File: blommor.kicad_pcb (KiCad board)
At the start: 2 copper layers, 66 parts, among them J1 ESP_PROG_UART, J101 Conn_01x03_Female, J102 Conn_01x03_Female, J103 Conn_01x03_Female, J104 Conn_01x03_Female, J105 Conn_01x03_Female, J2 ESP_PROG_JTAG, J3 Conn_01x02_Female, M1 Motor_DC, SW1 SW_Push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

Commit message: Added OST logo.
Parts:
- added SILKSCREEN1: OSTSymbol, SymbolOST:ost-bubble_12mm_SilkScreen, F.Cu at (114.6, 51.8)

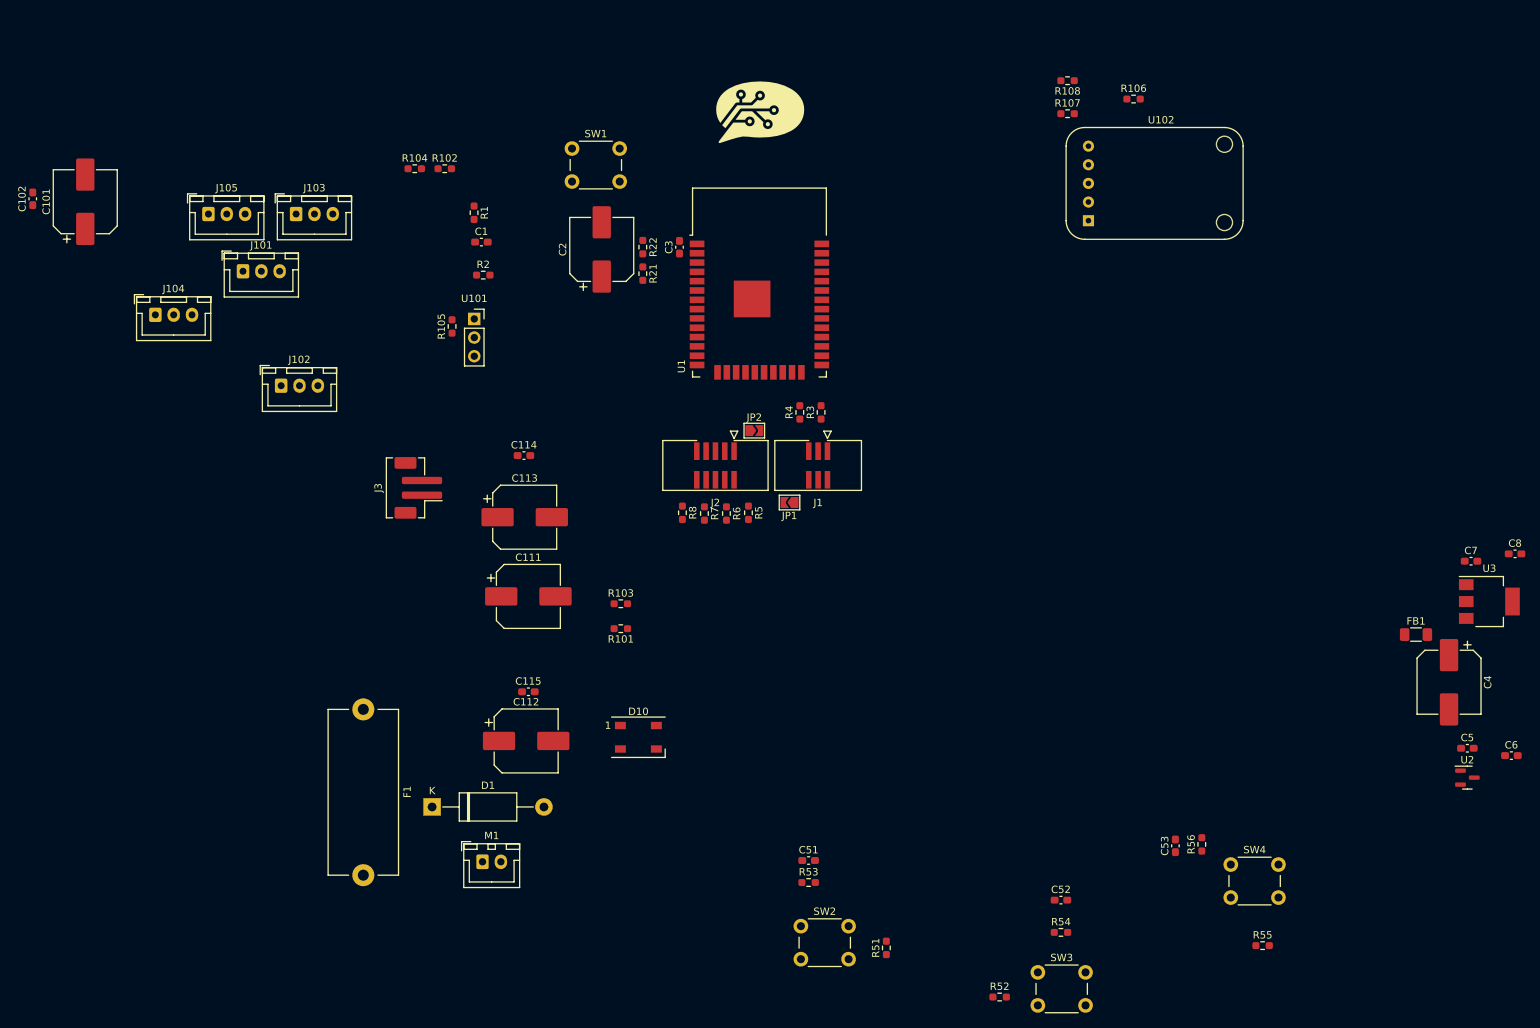
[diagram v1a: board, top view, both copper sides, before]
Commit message: Renamed ConnectorEsp folder so 3D models work. Started routing and more layout work.
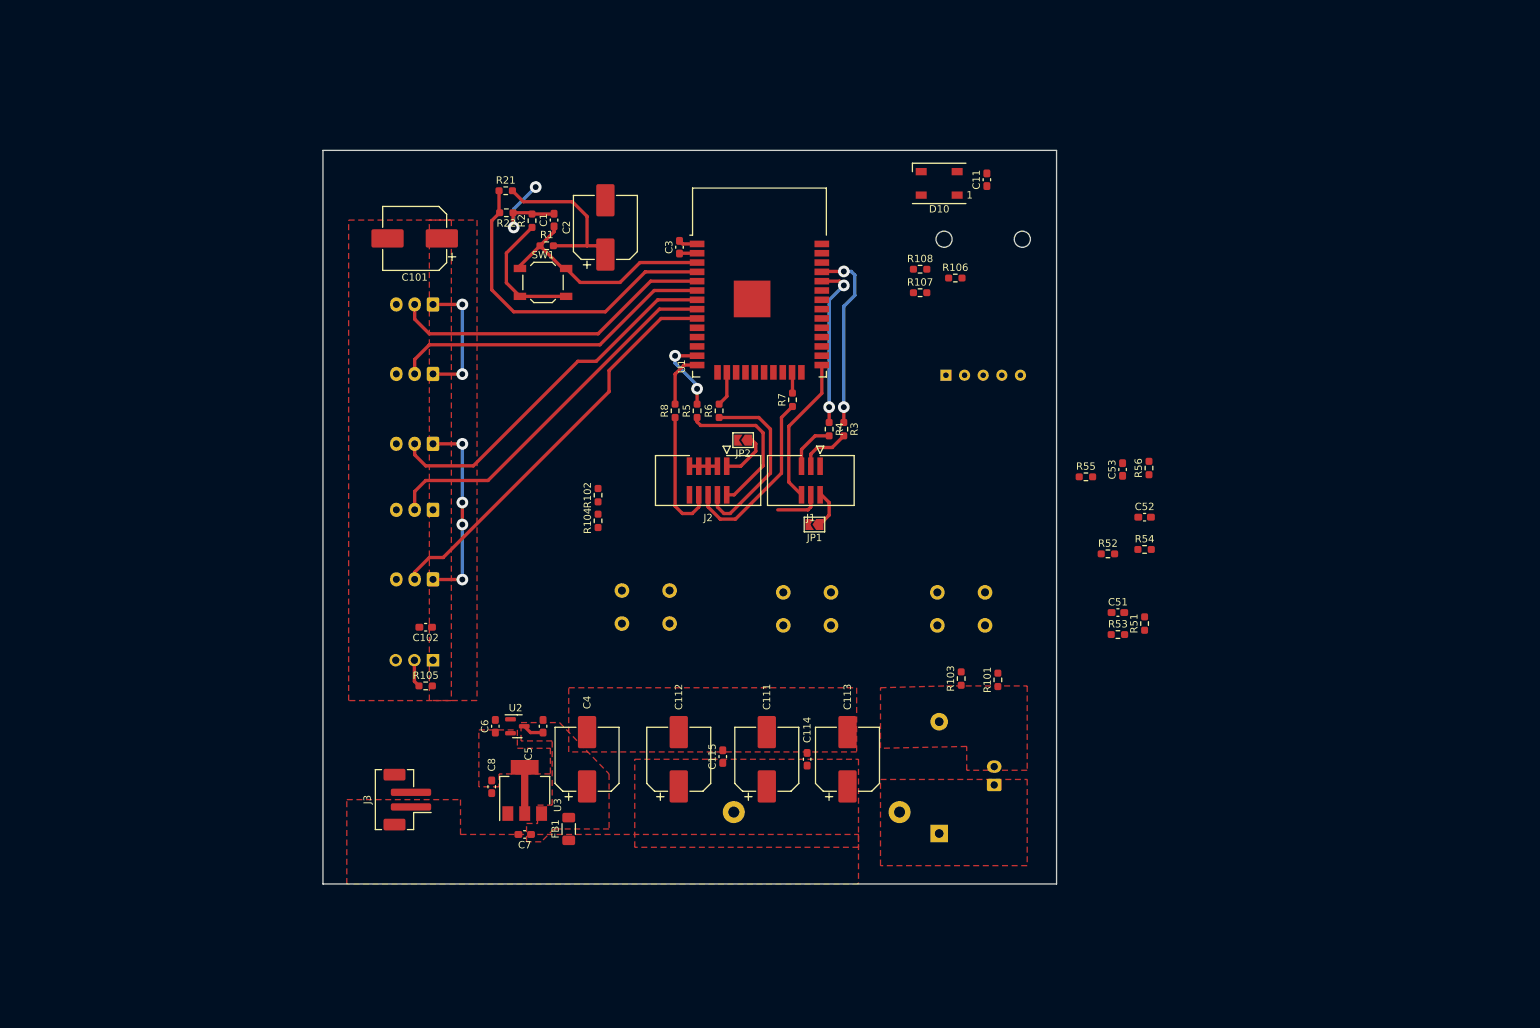
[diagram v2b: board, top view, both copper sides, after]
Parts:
- added C11: 100nF, Capacitor_SMD:C_0603_1608Metric_Pad1.08x0.95mm_HandSolder, F.Cu at (145.5, 61.0)
- D1, F1, J101, J102, J103, J104, J105, M1, SILKSCREEN1, SW2, SW3, SW4, U101, U102: moved to B.Cu
- SW1: footprint Button_Switch_THT:SW_PUSH_6mm_H5mm -> Button_Switch_SMD:SW_SPST_TL3342
- moved C8 143.1 mm to (78.0, 143.8), turned to -90 degrees
- moved C6 138.6 mm to (78.5, 135.5), turned to 90 degrees
- moved C7 134.3 mm to (82.5, 150.2), turned to 180 degrees
- moved U3 134.0 mm to (82.5, 144.2), turned to 90 degrees
- moved U2 129.7 mm to (81.5, 135.5)
- moved C5 126.0 mm to (85.0, 135.5), turned to 90 degrees
- moved FB1 118.5 mm to (88.5, 149.5), turned to 90 degrees
- moved C4 118.0 mm to (91.0, 140.0), turned to 90 degrees
- moved D10 85.9 mm to (139.0, 61.5), turned to 180 degrees
- moved C102 79.2 mm to (69.0, 122.0), turned to 180 degrees
- moved M1 70.5 mm to (146.5, 143.5), turned to 90 degrees
- moved D1 69.2 mm to (139.0, 150.1), turned to 90 degrees
- moved R55 68.3 mm to (159.0, 101.5)
- moved R52 62.2 mm to (162.0, 112.0)
- moved SW3 59.0 mm to (124.2, 117.2), turned to 180 degrees
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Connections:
- net /sensor_connector/VCC renamed /sensor_connector/SENS_VCC
- net Net-(R104-Pad1) renamed /SENSOR_POWER_EN
- U1 pad 26: unconnected-(U1-Pad26) -> MOTOR_ENABLE
- U1 pad 27: BTN_1 -> unconnected-(U1-Pad27)
- U1 pad 28: BTN_2 -> BTN_1
- U1 pad 29: unconnected-(U1-Pad29) -> BTN_2
- U1 pad 31: WS2812_DATA -> AUDIO_SD
- U1 pad 33: MOTOR_ENABLE -> ENABLE_AUDIO
- U1 pad 36: AUDIO_SD -> unconnected-(U1-Pad36)
- U1 pad 37: ENABLE_AUDIO -> WS2812_DATA
- U1 pad 6: /sensor_connector/SOIL3 -> /sensor_connector/SOIL4
- U1 pad 7: /sensor_connector/SOIL4 -> /sensor_connector/SOIL3
- U1 pad 8: /sensor_connector/SOIL1 -> /sensor_connector/SOIL2
- U1 pad 9: /sensor_connector/SOIL2 -> /sensor_connector/SOIL1
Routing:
- net /sensor_connector/SOIL1: track 0.00 -> 55.5 mm
- net /sensor_connector/SOIL2: track 0.00 -> 51.3 mm
- net /sensor_connector/SOIL3: track 0.00 -> 50.0 mm
- net Net-(U1-Pad4): track 0.00 -> 45.5 mm
- net /sensor_connector/SOIL4: track 0.00 -> 44.4 mm
- net /sensor_connector/SOIL5: track 0.00 -> 44.3 mm
- net /sensor_connector/SENS_VCC: track 0.00 -> 44.0 mm, vias 0 -> 6
- net RESET: track 0.00 -> 32.3 mm
- net +3V3: track 0.00 -> 31.9 mm
- net GND: track 0.00 -> 27.2 mm, vias 0 -> 2
- net TX: track 0.00 -> 25.4 mm, vias 0 -> 2
- net Net-(J2-Pad4): track 0.00 -> 25.2 mm
- net Net-(J2-Pad6): track 0.00 -> 24.6 mm
- net RX: track 0.00 -> 22.7 mm, vias 0 -> 2
- net Net-(J2-Pad2): track 0.00 -> 21.3 mm
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- added copper zone on F.Cu, net +3V3
- added copper zone on F.Cu, net /sensor_connector/SENS_VCC
- added copper zone on F.Cu, net GND
- added copper zone on F.Cu, net Net-(C4-Pad1)
- added copper zone on F.Cu, net Net-(D1-Pad1)
- added copper zone on F.Cu, net Net-(D1-Pad2)
- added copper zone on F.Cu, net VCC
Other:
- board outline added: 100 x 100 mm

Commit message: Typ klar nu.
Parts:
- added Q1: IPS021L, Package_TO_SOT_SMD:SOT-223-3_TabPin2, F.Cu at (129.5, 129.0)
- added Q101: A1SHB, Package_TO_SOT_SMD:SOT-23, F.Cu at (143.0, 85.0)
- added Q102: BST82-1, Package_TO_SOT_SMD:SOT-23, F.Cu at (136.5, 83.5)
- added Q2: A1SHB, Package_TO_SOT_SMD:SOT-23, F.Cu at (75.5, 118.0)
- C101, C111, C112, C113, C2, C4: footprint Capacitor_SMD:CP_Elec_8x10.5 -> Capacitor_SMD:CP_Elec_10x10.5
- moved R51 70.6 mm to (97.0, 112.5), turned to -90 degrees
- moved R53 69.9 mm to (93.5, 122.5), turned to -90 degrees
- moved C51 66.9 mm to (96.5, 122.5), turned to -90 degrees
- moved R54 52.8 mm to (115.5, 123.0), turned to -90 degrees
- moved C52 51.1 mm to (118.5, 123.0), turned to -90 degrees
- moved R52 43.0 mm to (119.0, 113.0), turned to -90 degrees
- moved R56 36.1 mm to (139.5, 123.0), turned to -90 degrees
- moved C53 35.5 mm to (136.5, 123.0), turned to -90 degrees
- moved R101 24.1 mm to (123.0, 126.5), turned to 0 degrees
- moved R55 22.4 mm to (139.5, 112.5), turned to -90 degrees
- moved R102 19.4 mm to (79.0, 118.0), turned to -90 degrees
- moved R103 18.5 mm to (123.5, 130.0)
- moved R104 14.8 mm to (79.0, 113.5), turned to -90 degrees
- moved R106 10.7 mm to (139.5, 85.0), turned to 90 degrees
- moved SW2 9.03 mm to (93.5, 119.2), turned to 0 degrees
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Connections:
- U1 pad 11: /sensor_connector/TEMPHUM -> /SENSOR_POWER_EN
- U1 pad 12: /SENSOR_POWER_EN -> /sensor_connector/TEMPHUM
- U1 pad 26: MOTOR_ENABLE -> BTN_1
- U1 pad 27: unconnected-(U1-Pad27) -> BTN_3
- U1 pad 28: BTN_1 -> MOTOR_ENABLE
- U1 pad 29: BTN_2 -> unconnected-(U1-Pad29)
- U1 pad 30: BTN_3 -> BTN_2
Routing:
- net +3V3: track 31.9 -> 222.6 mm, vias 0 -> 12
- net GND: track 27.2 -> 175.9 mm, vias 2 -> 10
- net VCC: track 0.00 -> 121.2 mm, vias 0 -> 2
- net BTN_1: track 0.00 -> 71.1 mm
- net /sensor_connector/TEMPHUM: track 3.76 -> 72.1 mm
- net BTN_2: track 0.00 -> 58.3 mm
- net MOTOR_ENABLE: track 0.00 -> 57.7 mm
- net AUDIO: track 0.00 -> 55.4 mm, vias 0 -> 2
- net BTN_3: track 0.00 -> 55.3 mm
- net RESET: track 32.3 -> 79.7 mm, vias 0 -> 2
- net /SENSOR_POWER_EN: track 0.00 -> 47.2 mm
- net AUDIO_SD: track 0.00 -> 39.0 mm, vias 0 -> 2
- net ENABLE_AUDIO: track 0.00 -> 28.7 mm
- net WS2812_DATA: track 0.00 -> 18.3 mm
- net Net-(Q101-Pad2): track 0.00 -> 11.5 mm
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
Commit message: Saker saker saker.... PALLA
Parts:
- added ?: , , F.Cu at (127.5, 134.5)
- added ?: , , F.Cu at (127.5, 44.5)
- added ?: , , F.Cu at (37.5, 44.5)
- added J51: Conn_01x01_Female, Connector_PinSocket_2.54mm:PinSocket_1x01_P2.54mm_Vertical, B.Cu at (98.5, 73.0)
- added J52: Conn_01x01_Female, Connector_PinSocket_2.54mm:PinSocket_1x01_P2.54mm_Vertical, B.Cu at (106.0, 64.0)
- added J53: Conn_01x01_Female, Connector_PinSocket_2.54mm:PinSocket_1x01_P2.54mm_Vertical, B.Cu at (106.5, 55.5)
- added J54: Conn_01x03_Female, Connector_PinSocket_2.54mm:PinSocket_1x03_P2.54mm_Vertical, B.Cu at (64.0, 111.0)
- added J55: Conn_01x02_Female, Connector_PinSocket_2.54mm:PinSocket_1x02_P2.54mm_Vertical, B.Cu at (65.2, 92.5)
- added J56: Conn_01x02_Female, Connector_PinSocket_2.54mm:PinSocket_1x02_P2.54mm_Vertical, B.Cu at (76.2, 133.5)
- added REF**: MountingHole_3.2mm_M3_Pad, MountingHole:MountingHole_3.2mm_M3_Pad, F.Cu at (37.5, 134.5)
- added ost-bubble_12mm_Copper: G***, SymbolOST:ost-bubble_12mm_Copper, F.Cu at (84.0, 108.0)
- moved SILKSCREEN1 48.8 mm to (82.5, 30.7)
- moved C53 34.9 mm to (108.0, 102.9)
- moved R56 34.9 mm to (111.0, 102.9)
- moved J3 33.6 mm to (41.2, 123.4)
- moved F1 28.8 mm to (87.5, 130.5)
- moved R2 28.5 mm to (61.0, 49.1)
- moved C1 28.5 mm to (64.0, 49.0)
- moved C101 28.5 mm to (45.0, 51.5)
- moved C102 28.5 mm to (46.5, 104.5)
- moved C111 28.5 mm to (92.0, 122.5)
- moved C112 28.5 mm to (79.0, 122.5)
- moved C113 28.5 mm to (105.0, 122.5)
- moved C114 28.5 mm to (98.5, 122.5)
- moved C2 28.5 mm to (71.0, 47.8)
- moved C3 28.5 mm to (81.1, 52.7)
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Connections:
- U1 pad 24: unconnected-(U1-Pad24) -> Net-(J51-Pad1)
- U1 pad 29: unconnected-(U1-Pad29) -> Net-(J52-Pad1)
- U1 pad 36: unconnected-(U1-Pad36) -> Net-(J53-Pad1)
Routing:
- net GND: track 175.9 -> 156.6 mm
- net Net-(J53-Pad1): track 0.00 -> 6.29 mm
- net Net-(J52-Pad1): track 0.00 -> 5.63 mm
- net VCC: track 121.2 -> 124.8 mm
- net Net-(J51-Pad1): track 0.00 -> 3.57 mm
- net BTN_2: track 58.3 -> 61.8 mm
- net ENABLE_AUDIO: track 28.7 -> 25.2 mm
- net +3V3: track 222.6 -> 225.7 mm
- net AUDIO: track 55.4 -> 53.7 mm
- net Net-(J2-Pad6): track 24.6 -> 26.1 mm
- net /sensor_connector/TEMPHUM: track 72.1 -> 70.8 mm
- net BTN_3: track 55.3 -> 54.7 mm
- net TDI: track 7.60 -> 7.02 mm
- net MOTOR_ENABLE: track 57.7 -> 57.2 mm
